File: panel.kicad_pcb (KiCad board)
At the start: 2 copper layers, 114.4 x 108.6 mm, 592 parts, among them J1 HRO-TYPE-C-31-M-12, J2 Conn_01x04

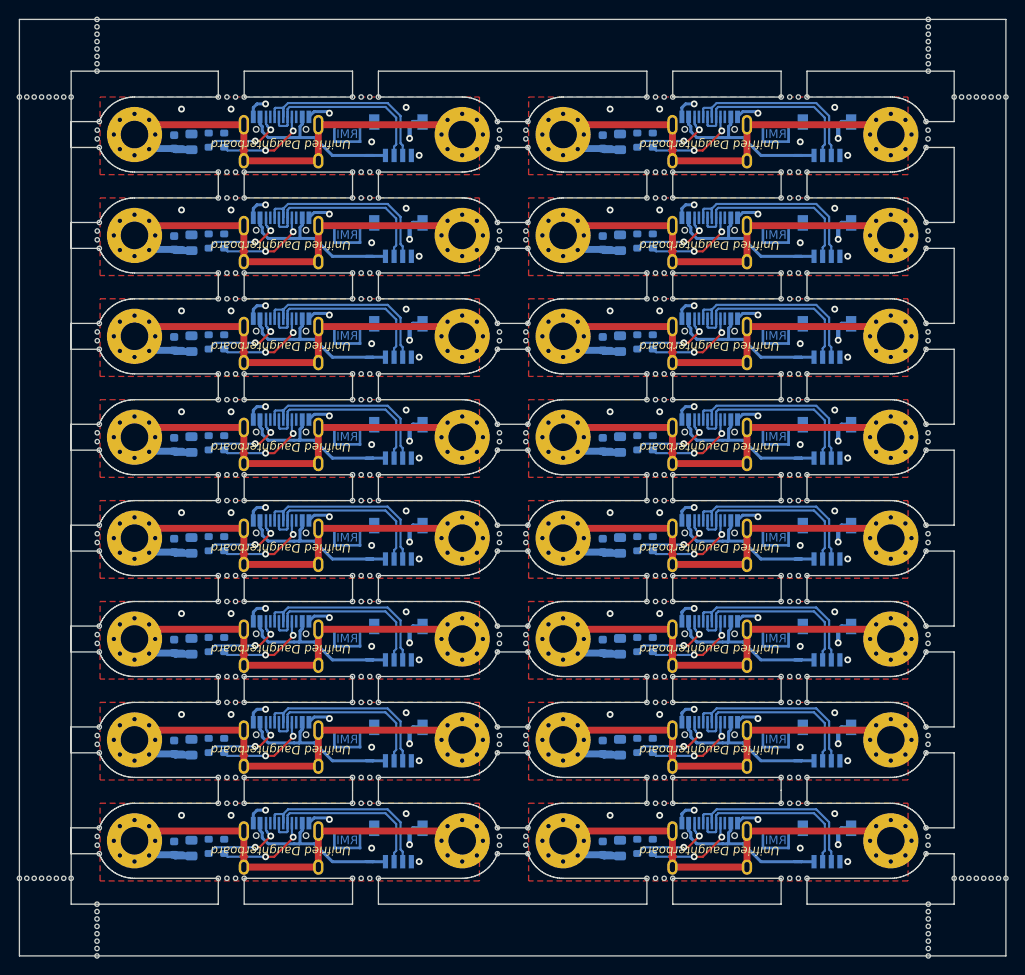
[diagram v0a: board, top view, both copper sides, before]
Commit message: Update fill in panel
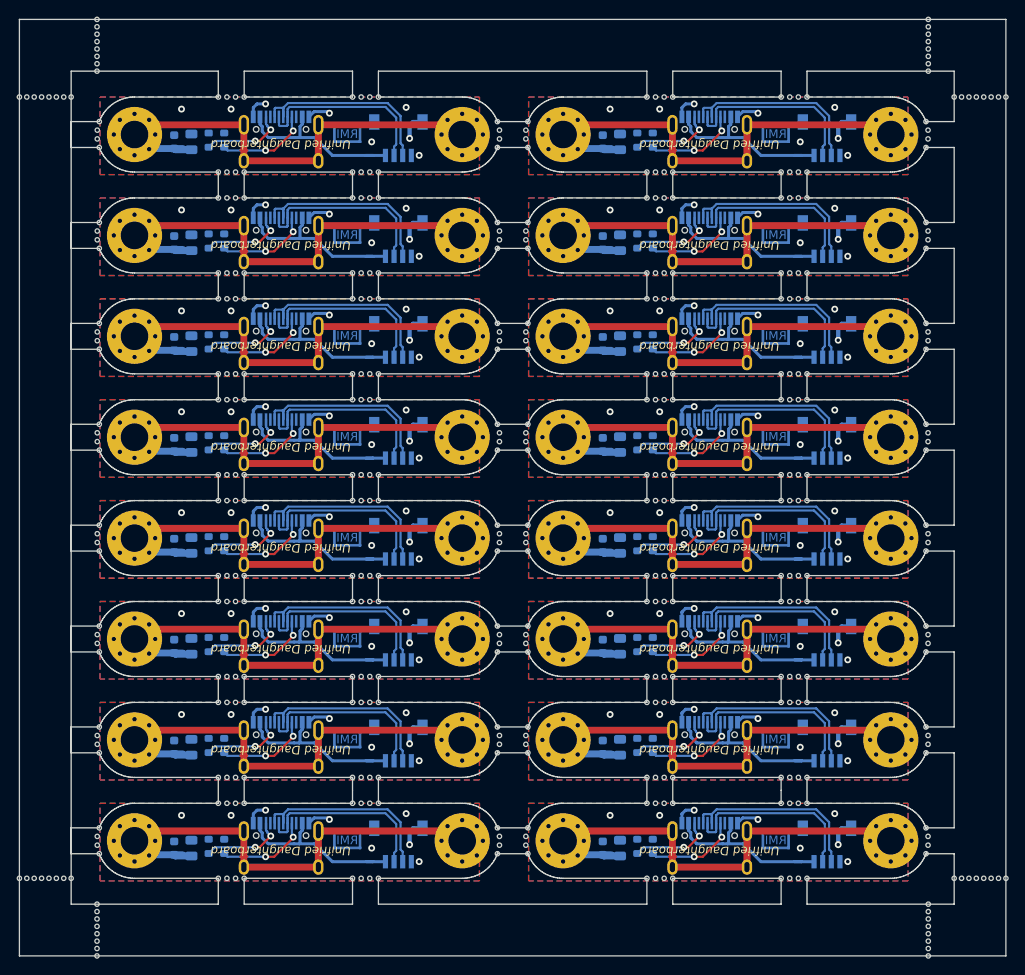
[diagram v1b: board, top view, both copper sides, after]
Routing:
- added copper zone on B.Cu, net Board_0-GND
- added copper zone on B.Cu, net Board_1-GND
- added copper zone on B.Cu, net Board_10-GND
- added copper zone on B.Cu, net Board_11-GND
- added copper zone on B.Cu, net Board_12-GND
- added copper zone on B.Cu, net Board_13-GND
- added copper zone on B.Cu, net Board_14-GND
- added copper zone on B.Cu, net Board_15-GND
- added copper zone on B.Cu, net Board_2-GND
- added copper zone on B.Cu, net Board_3-GND
- added copper zone on B.Cu, net Board_4-GND
- added copper zone on B.Cu, net Board_5-GND
- added copper zone on B.Cu, net Board_6-GND
- added copper zone on B.Cu, net Board_7-GND
- added copper zone on B.Cu, net Board_8-GND
- added copper zone on B.Cu, net Board_9-GND
